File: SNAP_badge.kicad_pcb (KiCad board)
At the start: 2 copper layers, 63.5 x 127 mm, 149 parts, among them P1 MicroB, P2 CONN_01X08, P3 CONN_01X08, P4 CONN_01X10, P5 CONN_01X06, P6 CONN_02X03, Q1 ZXMN2F30FHCT-ND, Q2 Si2305DS, SW1 SWITCH_DPDT, SW2 SW_PUSH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

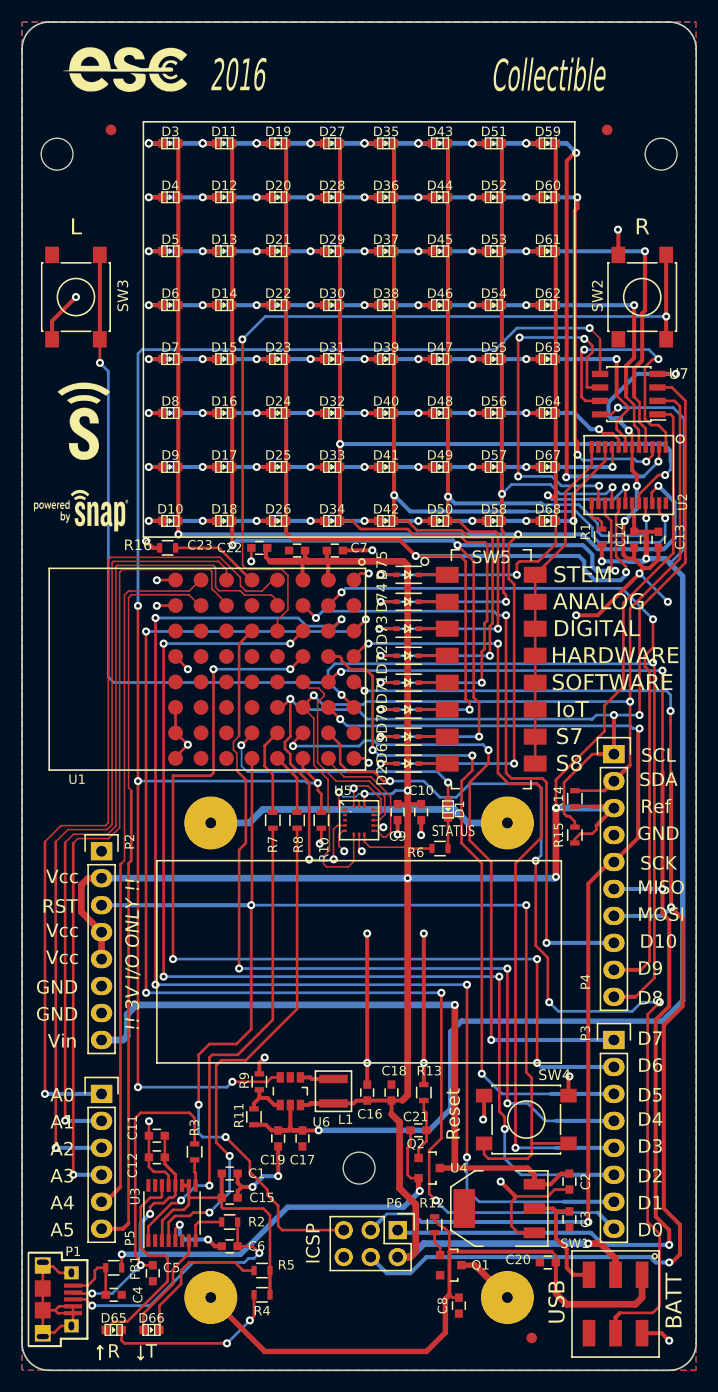
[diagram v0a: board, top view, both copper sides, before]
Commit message: Fixed LED silkscreen, added logos
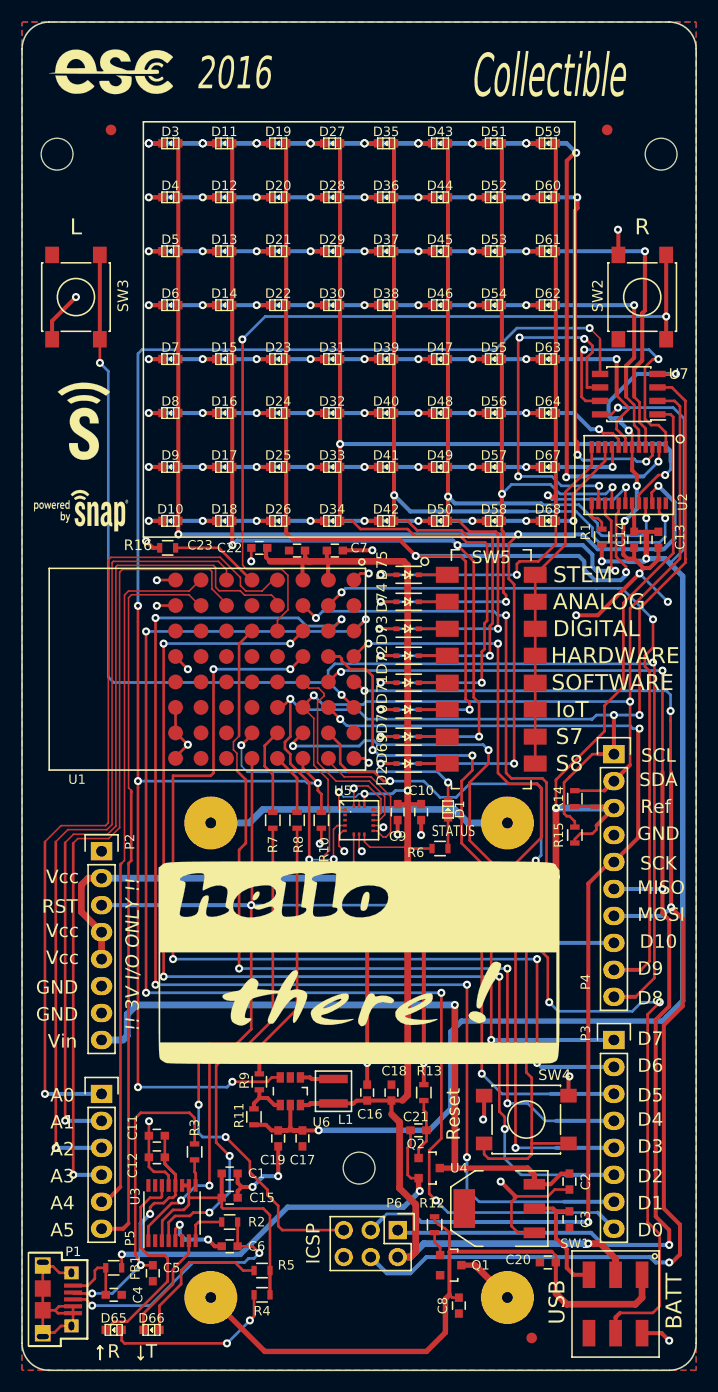
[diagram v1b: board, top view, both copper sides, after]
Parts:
- added ?: , Added:OSHW_logo, B.Cu at (175.3, 38.2)
- added ?: LOGO, Added:Python_logo, B.Cu at (191.5, 49.7)
- added ?: LOGO, Added:Synapse_logo, B.Cu at (191.6, 41.3)
- added ?: LOGO, Added:Screaming_logo, B.Cu at (158.9, 41.9)
- added ?: LOGO, Added:Sunstone_logo, B.Cu at (161.8, 50.0)
- added ?: LOGO, Added:UBM_logo, B.Cu at (158.4, 28.2)
- added ?: LOGO, Added:Hello, F.Cu at (175.1, 110.2)
- added ?: , Added:ESC_logo, B.Cu at (192.7, 27.3)
- moved ? 1.34 mm to (151.8, 26.3)
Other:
- board text added: "All design files and source code available at: https://bitly.com/????"
- board text added: "Concept by Max the Magnificent"
- board text added: "Design and RF Engine by Synapse Wireless, Inc."
- board text added: "Designed to be HACKED Let us know what you create!"
- board text added: "For evaluation only; not FCC approved for resale"
- board text added: "SNAP Badge 2016 REV B"
- board text removed: "SNAP Badge 2016 REV A"

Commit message: Update silkscreen with logos, etc.
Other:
- board text added: "All design files and source code available at:"
- board text added: "http://ubm.io/1Smqysr"
- board text removed: "All design files and source code available at: https://bitly.com/????"
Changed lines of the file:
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@@
     (area 143.434999 21.514999 207.085001 148.665001)
     (thickness 1.6)
-    (drawings 92)
+    (drawings 93)
     (tracks 1782)
     (zones 0)
@@
   )
   (layers
-    (0 F.Cu signal hide)
-    (31 B.Cu signal hide)
-    (32 B.Adhes user hide)
-    (33 F.Adhes user hide)
+    (0 F.Cu signal)
+    (31 B.Cu signal)
+    (32 B.Adhes user)
+    (33 F.Adhes user)
     (34 B.Paste user)
     (35 F.Paste user)
     (36 B.SilkS user)
-    (37 F.SilkS user hide)
+    (37 F.SilkS user)
     (38 B.Mask user)
     (39 F.Mask user)
@@
     )
   )
+  (gr_text http://ubm.io/1Smqysr (at 174.9044 76.0476) (layer B.SilkS)
+    (effects (font (size 2.032 2.032) (thickness 0.3048)) (justify mirror))
+  )
   (gr_text "Designed to be HACKED\nLet us know what you create!" (at 175.2346 83.0326) (layer B.SilkS)
     (effects (font (thickness 0.3048) italic) (justify mirror))
@@
     (effects (font (size 1.016 1.016) (thickness 0.1524)) (justify mirror))
   )
-  (gr_text "Design and RF Engine by Synapse Wireless, Inc." (at 175.514 56.642) (layer B.SilkS)
+  (gr_text "Design and RF Engine by Synapse Wireless, Inc." (at 175.5902 60.8076) (layer B.SilkS)
     (effects (font (thickness 0.3048) italic) (justify mirror))
   )
-  (gr_text "Concept by Max the Magnificent" (at 175.133 60.579) (layer B.SilkS)
+  (gr_text "Concept by Max the Magnificent" (at 175.2346 56.8198) (layer B.SilkS)
     (effects (font (thickness 0.3048) italic) (justify mirror))
   )
-  (gr_text "All design files and source code available at:\nhttps://bitly.com/????" (at 174.5996 75.311) (layer B.SilkS)
+  (gr_text "All design files and source code available at:" (at 174.5742 72.5932) (layer B.SilkS)
     (effects (font (thickness 0.3048) italic) (justify mirror))
   )
